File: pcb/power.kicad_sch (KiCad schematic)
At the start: 0 parts

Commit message: Added Cockpit and Power sheets.
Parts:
- added C36: 470μF, symbol Device:C
- added C37, C38, C45, C46, C53, C54: 10μF, symbol Device:C
- added C39, C44, C47, C52, C84, C89: 100nF, symbol Device:C
- added C40, C48, C85: 10nF, symbol Device:C
- added C41: 33pF, symbol Device:C
- added C42, C43, C50, C51, C87, C88: 22μF, symbol Device:C
- added C49, C86: 30pF, symbol Device:C
- added D22: BZT52C10, symbol Device:D_Zener
- added F1: 15 A, symbol Device:Fuse
- added J13: XT60, symbol Connector_Generic:Conn_01x02
- added J14, J16, J17, J18, J19: Conn_01x02, symbol Connector_Generic:Conn_01x02
- added L2: 6.8μH, symbol Device:L
- added L4: 4.7μH, symbol Device:L
- added L5: 3.3μH, symbol Device:L
- added Q1: IPD90P03P4L-04-HXY, Package_TO_SOT_SMD:TO-252-2, symbol Transistor_FET:QM6015D
- added R23, R27, R42, R44, R47, R50, R51, R53: 10kΩ, symbol Device:R_US
- added R24, R43, R49: 47kΩ, symbol Device:R_US
- added R37, R45: 30kΩ, symbol Device:R_US
- added R40: 348kΩ, symbol Device:R_US
- added R41, R48, R54: 0Ω, symbol Device:R_US
- added R46: 220kΩ, symbol Device:R_US
- added R52: 45.3kΩ, symbol Device:R_US
- added TP61, TP62, TP63, TP64, TP65, TP66, TP67, TP68, TP69, TP70: TestPoint, symbol Connector:TestPoint
- added U10, U11, U12: TPS564252DRLR, Package_TO_SOT_SMD:SOT-563, symbol Buck Converter:TPS564252DRLR
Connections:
- new net: C85.1, J18.2 (Pin_2), R49.2, R50.1, U12.5 (EN)
- new net: C41.1, R37.2, R40.1, U10.6 (FB)
- new net: C41.2, R40.2, R41.1
- new net: C49.1, R45.2, R46.1, U11.6 (FB)
- new net: C49.2, R46.2, R48.1
- new net: C40.1, J14.2 (Pin_2), R24.2, R27.1, U10.5 (EN)
- new net: D22.2 (A), Q1.1 (G), R23.1
- new net: F1.1, J13.2 (Pin_2)
- new net: C48.1, J16.2 (Pin_2), R43.2, R44.1, U11.5 (EN)
- new net: J17.2 (Pin_2), R47.2
- new net: J19.2 (Pin_2), R53.2
- new net: F1.2, Q1.2 (D)
- new net: C86.2, R52.2, R54.1
- new net: C86.1, R51.2, R52.1, U12.6 (FB)
- new net +12V: C36.1, C37.1, C38.1, C39.1, C45.1, C46.1, C47.1, C53.1, C54.1, C84.1, D22.1 (K), Q1.3 (S), R24.1, R43.1, R49.1, TP64.1, U10.1 (VIN), U11.1 (VIN), U12.1 (VIN)
- new net +3V3: C87.1, C88.1, C89.1, J19.1 (Pin_1), L5.2, R42.2, R54.2, TP61.1
- new net +5V: C50.1, C51.1, C52.1, J17.1 (Pin_1), L4.2, R48.2, TP62.1
- new net +7.5V: C42.1, C43.1, C44.1, L2.2, R41.2, TP63.1
- new net GND: C36.2, C37.2, C38.2, C39.2, C40.2, C42.2, C43.2, C44.2, C45.2, C46.2, C47.2, C48.2, C50.2, C51.2, C52.2, C53.2, C54.2, C84.2, C85.2, C87.2, C88.2, C89.2, J13.1 (Pin_1), J14.1 (Pin_1), J16.1 (Pin_1), J18.1 (Pin_1), R23.2, R27.2, R37.1, R44.2, R45.1, R50.2, R51.1, TP65.1, TP66.1, TP67.1, U10.3 (GND), U11.3 (GND), U12.3 (GND)
- new net PG_3.3: R53.1, TP70.1, U12.4 (PG)
- new net PG_5: R47.1, TP69.1, U11.4 (PG)
- new net PG_7.5: R42.1, TP68.1, U10.4 (PG)
- new net SW_3.3: L5.1, U12.2 (SW)
- new net SW_5: L4.1, U11.2 (SW)
- new net SW_7.5: L2.1, U10.2 (SW)

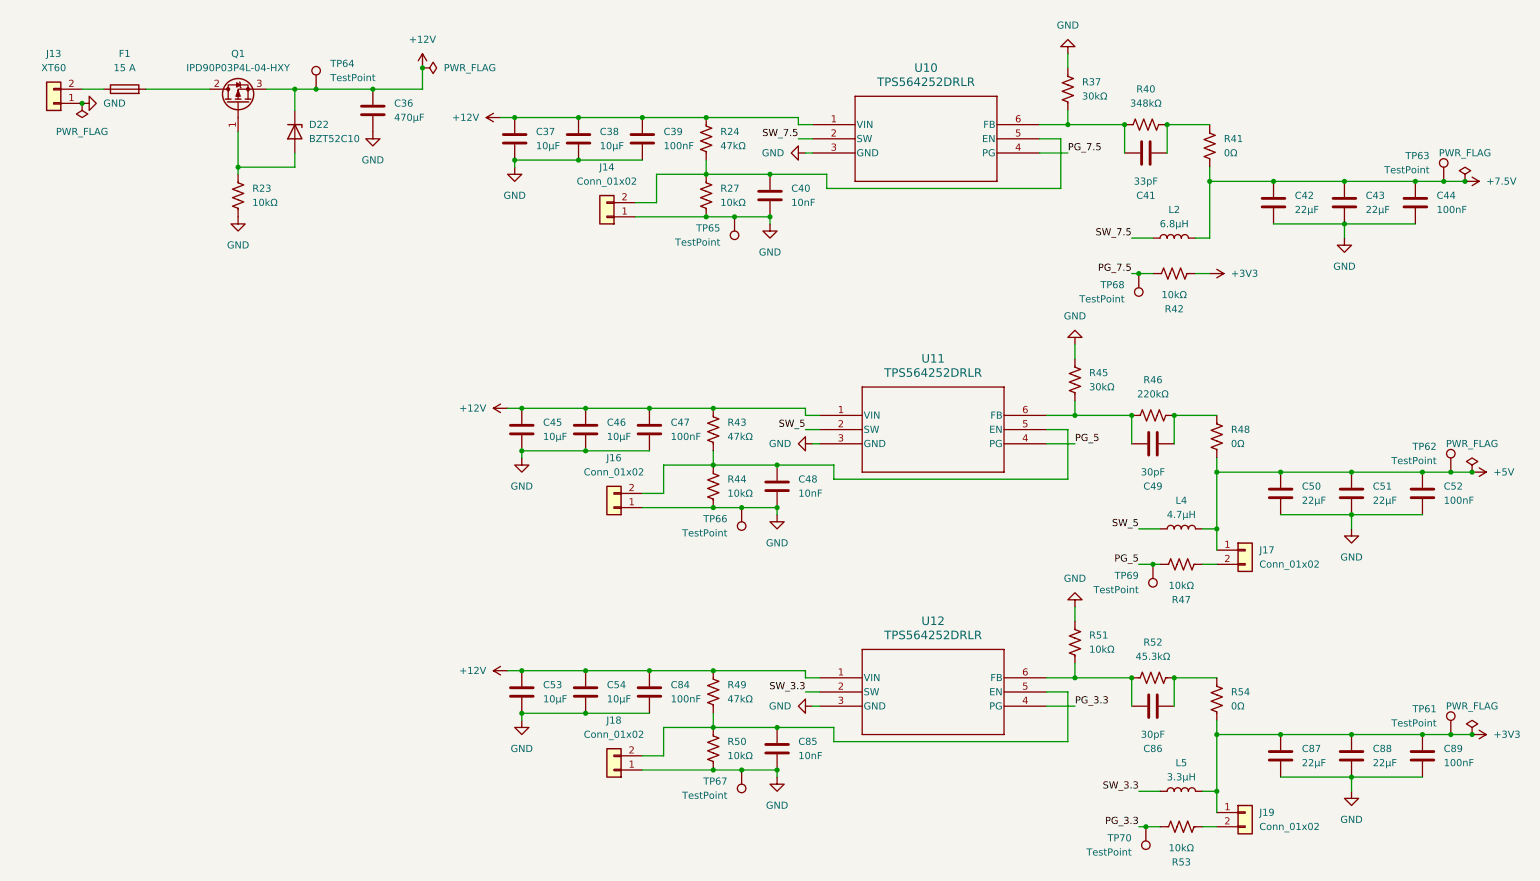
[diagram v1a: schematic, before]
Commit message: Added footprints to all components.
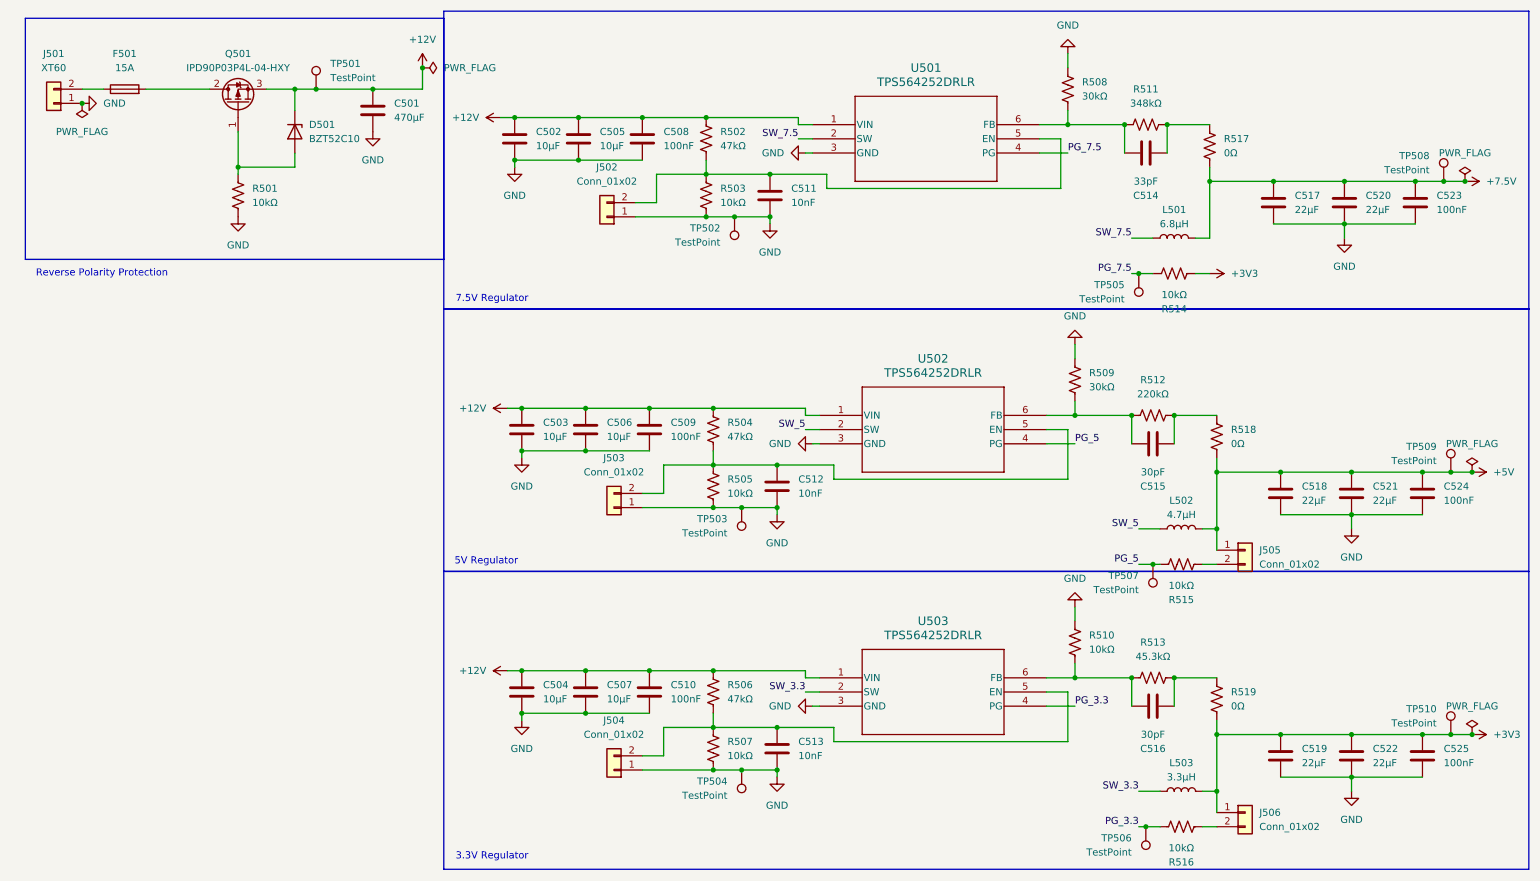
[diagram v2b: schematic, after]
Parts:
- C501: renamed from C36; footprint (none) -> Capacitor_SMD:CP_Elec_8x11.9
- C502: renamed from C37; footprint (none) -> Capacitor_SMD:C_0805_2012Metric
- C503: renamed from C45; footprint (none) -> Capacitor_SMD:C_0805_2012Metric
- C504: renamed from C53; footprint (none) -> Capacitor_SMD:C_0805_2012Metric
- C505: renamed from C38; footprint (none) -> Capacitor_SMD:C_0805_2012Metric
- C506: renamed from C46; footprint (none) -> Capacitor_SMD:C_0805_2012Metric
- C507: renamed from C54; footprint (none) -> Capacitor_SMD:C_0805_2012Metric
- C508: renamed from C39; footprint (none) -> Capacitor_SMD:C_0603_1608Metric
- C509: renamed from C47; footprint (none) -> Capacitor_SMD:C_0603_1608Metric
- C510: renamed from C84; footprint (none) -> Capacitor_SMD:C_0603_1608Metric
- C511: renamed from C40; footprint (none) -> Capacitor_SMD:C_0603_1608Metric
- C512: renamed from C48; footprint (none) -> Capacitor_SMD:C_0603_1608Metric
- C513: renamed from C85; footprint (none) -> Capacitor_SMD:C_0603_1608Metric
- C514: renamed from C41; footprint (none) -> Capacitor_SMD:C_0603_1608Metric
- C515: renamed from C49; footprint (none) -> Capacitor_SMD:C_0603_1608Metric
- C516: renamed from C86; footprint (none) -> Capacitor_SMD:C_0603_1608Metric
- C517: renamed from C42; footprint (none) -> Capacitor_SMD:C_0805_2012Metric
- C518: renamed from C50; footprint (none) -> Capacitor_SMD:C_0805_2012Metric
- C519: renamed from C87; footprint (none) -> Capacitor_SMD:C_0805_2012Metric
- C520: renamed from C43; footprint (none) -> Capacitor_SMD:C_0805_2012Metric
- C521: renamed from C51; footprint (none) -> Capacitor_SMD:C_0805_2012Metric
- C522: renamed from C88; footprint (none) -> Capacitor_SMD:C_0805_2012Metric
- C523: renamed from C44; footprint (none) -> Capacitor_SMD:C_0603_1608Metric
- C524: renamed from C52; footprint (none) -> Capacitor_SMD:C_0603_1608Metric
- C525: renamed from C89; footprint (none) -> Capacitor_SMD:C_0603_1608Metric
- D501: renamed from D22; footprint (none) -> Diode_SMD:D_SOD-123
- F501: renamed from F1; value 15 A -> 15A; footprint (none) -> Fuse:Fuseholder_Blade_Mini_Keystone_3568
- J501: renamed from J13; footprint (none) -> Connector_AMASS:AMASS_XT60-M_1x02_P7.20mm_Vertical
- J502: renamed from J14; footprint (none) -> Connector_PinHeader_2.54mm:PinHeader_1x02_P2.54mm_Vertical
- J503: renamed from J16; footprint (none) -> Connector_PinHeader_2.54mm:PinHeader_1x02_P2.54mm_Vertical
- J504: renamed from J18; footprint (none) -> Connector_PinHeader_2.54mm:PinHeader_1x02_P2.54mm_Vertical
- J505: renamed from J17; footprint (none) -> Connector_PinHeader_2.54mm:PinHeader_1x02_P2.54mm_Vertical
- J506: renamed from J19; footprint (none) -> Connector_PinHeader_2.54mm:PinHeader_1x02_P2.54mm_Vertical
- L501: renamed from L2; footprint (none) -> Inductor_SMD:L_Sunlord_MWSA0603S
- L502: renamed from L4; footprint (none) -> Inductor_SMD:L_Sunlord_MWSA0603S
- L503: renamed from L5; footprint (none) -> Inductor_SMD:L_Sunlord_MWSA0603S
- R501: renamed from R23; footprint (none) -> Resistor_SMD:R_0603_1608Metric
- R502: renamed from R24; footprint (none) -> Resistor_SMD:R_0603_1608Metric
- R503: renamed from R27; footprint (none) -> Resistor_SMD:R_0603_1608Metric
- R504: renamed from R43; footprint (none) -> Resistor_SMD:R_0603_1608Metric
- R505: renamed from R44; footprint (none) -> Resistor_SMD:R_0603_1608Metric
- R506: renamed from R49; footprint (none) -> Resistor_SMD:R_0603_1608Metric
- R507: renamed from R50; footprint (none) -> Resistor_SMD:R_0603_1608Metric
- R508: renamed from R37; footprint (none) -> Resistor_SMD:R_0603_1608Metric
- R509: renamed from R45; footprint (none) -> Resistor_SMD:R_0603_1608Metric
- R510: renamed from R51; footprint (none) -> Resistor_SMD:R_0603_1608Metric
- R511: renamed from R40; footprint (none) -> Resistor_SMD:R_0603_1608Metric
- R512: renamed from R46; footprint (none) -> Resistor_SMD:R_0603_1608Metric
- R513: renamed from R52; footprint (none) -> Resistor_SMD:R_0603_1608Metric
- R514: renamed from R42; footprint (none) -> Resistor_SMD:R_0603_1608Metric
- R515: renamed from R47; footprint (none) -> Resistor_SMD:R_0603_1608Metric
- R516: renamed from R53; footprint (none) -> Resistor_SMD:R_0603_1608Metric
- R517: renamed from R41; footprint (none) -> Resistor_SMD:R_0603_1608Metric
- R518: renamed from R48; footprint (none) -> Resistor_SMD:R_0603_1608Metric
- R519: renamed from R54; footprint (none) -> Resistor_SMD:R_0603_1608Metric
- TP501: renamed from TP64; footprint (none) -> TestPoint:TestPoint_Keystone_5015_Micro_Mini
- TP502: renamed from TP65; footprint (none) -> TestPoint:TestPoint_Keystone_5015_Micro_Mini
- TP503: renamed from TP66; footprint (none) -> TestPoint:TestPoint_Keystone_5015_Micro_Mini
- TP504: renamed from TP67; footprint (none) -> TestPoint:TestPoint_Keystone_5015_Micro_Mini
- TP505: renamed from TP68; footprint (none) -> TestPoint:TestPoint_Keystone_5015_Micro_Mini
- TP506: renamed from TP70; footprint (none) -> TestPoint:TestPoint_Keystone_5015_Micro_Mini
- TP507: renamed from TP69; footprint (none) -> TestPoint:TestPoint_Keystone_5015_Micro_Mini
- TP508: renamed from TP63; footprint (none) -> TestPoint:TestPoint_Keystone_5015_Micro_Mini
- TP509: renamed from TP62; footprint (none) -> TestPoint:TestPoint_Keystone_5015_Micro_Mini
- TP510: renamed from TP61; footprint (none) -> TestPoint:TestPoint_Keystone_5015_Micro_Mini
- renumbered Q1 to Q501, U10 to U501, U11 to U502, U12 to U503
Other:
- note added: "3.3V Regulator"
- note added: "5V Regulator"
- note added: "7.5V Regulator"
- note added: "Reverse Polarity Protection"

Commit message: Added CAN Bus connectors and finalized schematic with BOM, LCSC #s, and links to parts.
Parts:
- C501: footprint Capacitor_SMD:CP_Elec_8x11.9 -> Capacitor_SMD:CP_Elec_10x12.6; LCSC (none) -> C1517666; MPN (none) -> A768MS477M1ELAE017; Manufacturer (none) -> KEMET
- C502, C503, C504, C505, C506, C507: LCSC (none) -> C15850; MPN (none) -> CL21A106KAYNNNE; Manufacturer (none) -> Samsung
- C508, C509, C510: LCSC (none) -> C14663; MPN (none) -> CC0603KRX7R9BB104; Manufacturer (none) -> YAGEO
- C511, C512, C513: LCSC (none) -> C1589; MPN (none) -> CL10B103KB8NNNC; Manufacturer (none) -> Samsung
- C514: LCSC (none) -> C107047; MPN (none) -> CC0603JRNPO9BN330; Manufacturer (none) -> YAGEO
- C515, C516: LCSC (none) -> C113797; MPN (none) -> CC0603JRNPO9BN300; Manufacturer (none) -> YAGEO
- C517, C518, C519, C520, C521, C522: LCSC (none) -> C162295; MPN (none) -> GRM219R61C226ME15L; Manufacturer (none) -> Murata
- C523, C524, C525: LCSC (none) -> C18522636; MPN (none) -> KGM15AR71C104KT; Manufacturer (none) -> KYOCERA AVX
- D501: LCSC (none) -> C173431; MPN (none) -> BZT52C10
- F501: LCSC (none) -> C5249699; MPN (none) -> 3568; Manufacturer (none) -> Keystone Electronics
- J501: LCSC (none) -> C98733; MPN (none) -> FIT0587; Manufacturer (none) -> DFRobot
- J502, J503, J504, J505, J506: LCSC (none) -> C492401; MPN (none) -> PZ254V-11-02P
- L501: LCSC (none) -> C408449; MPN (none) -> MWSA0603S-6R8MT; Manufacturer (none) -> Sunlord
- L502: LCSC (none) -> C408447; MPN (none) -> MWSA0603S-4R7MT; Manufacturer (none) -> Sunlord
- L503: LCSC (none) -> C408446; MPN (none) -> MWSA0603S-3R3MT; Manufacturer (none) -> Sunlord
- Q501: LCSC (none) -> C20606270; MPN (none) -> IPD90P03P4L-04; Manufacturer (none) -> HXY MOSFET
- R501, R503, R505, R507, R510, R514, R515, R516: LCSC (none) -> C844918; MPN (none) -> CRCW060310K0FKEA; Manufacturer (none) -> Vishay Dale
- R502, R504, R506: LCSC (none) -> C105579; MPN (none) -> RC0603FR-0747KL; Manufacturer (none) -> YAGEO
- R508, R509: LCSC (none) -> C22984; MPN (none) -> 0603WAF3002T5E; Manufacturer (none) -> UNI-ROYAL
- R511: LCSC (none) -> C23006; MPN (none) -> 0603WAF3483T5E; Manufacturer (none) -> UNI-ROYAL
- R512: LCSC (none) -> C22961; MPN (none) -> 0603WAF2203T5E; Manufacturer (none) -> UNI-ROYAL
- R513: LCSC (none) -> C23058; MPN (none) -> 0603WAF4532T5E; Manufacturer (none) -> UNI-ROYAL
- R517, R518, R519: LCSC (none) -> C95177; MPN (none) -> RC0603JR-070RL; Manufacturer (none) -> YAGEO
- TP501, TP502, TP503, TP504, TP505, TP506, TP507, TP508, TP509, TP510: LCSC (none) -> C2906768; MPN (none) -> 5015; Manufacturer (none) -> Keystone Electronics
- U501, U502, U503: LCSC (none) -> C19191267; MPN (none) -> TPS564252DRLR; Manufacturer (none) -> Texas Instruments
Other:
- company: (none) -> 18-649 Lab 4: Controller PCB
- title: (none) -> Power: Battery Input and Regulators
